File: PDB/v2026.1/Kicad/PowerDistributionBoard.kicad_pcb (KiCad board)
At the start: 2 copper layers, 184.8 x 112.4 mm, 78 parts, among them J1 12V_EXP3, J10 BMS, J11 IMD, J12 Suspension_Linear_Pot1, J13 Suspension_Linear_Pot2, J14 Suspension_Linear_Pot3, J15 Suspension_Linear_Pot4, J16 CCM_Faults, J17 EXP1_5V, J18 RasPI_5V, J19 LATCH_12V, J2 12V_EXP2, J20 Throttle_Sensor, J21 Current_Sensor, J22 Brake_Sensor1, J23 Brake_Sensor2, J24 Wheel_Sensor1, J25 Wheel_Sensor2, J26 3V3_EXP, J27 BATTERY_12V, J28 BATTERY_GND, J29 BATTERY_24V, J3 12V_EXP1, J31 FAN1_24V, J32 FAN2_24V, J33 PUMP1_24V, J34 PUMP2_24V, J35 24V_EXP1, J4 RTM, J5 CCM_12V, J7 BSPD, J8 LATCH, J9 TSSI, M3 MountingHole M3, U1 5to3.3_Linear_Regulator, U2 TLV76150DCYR

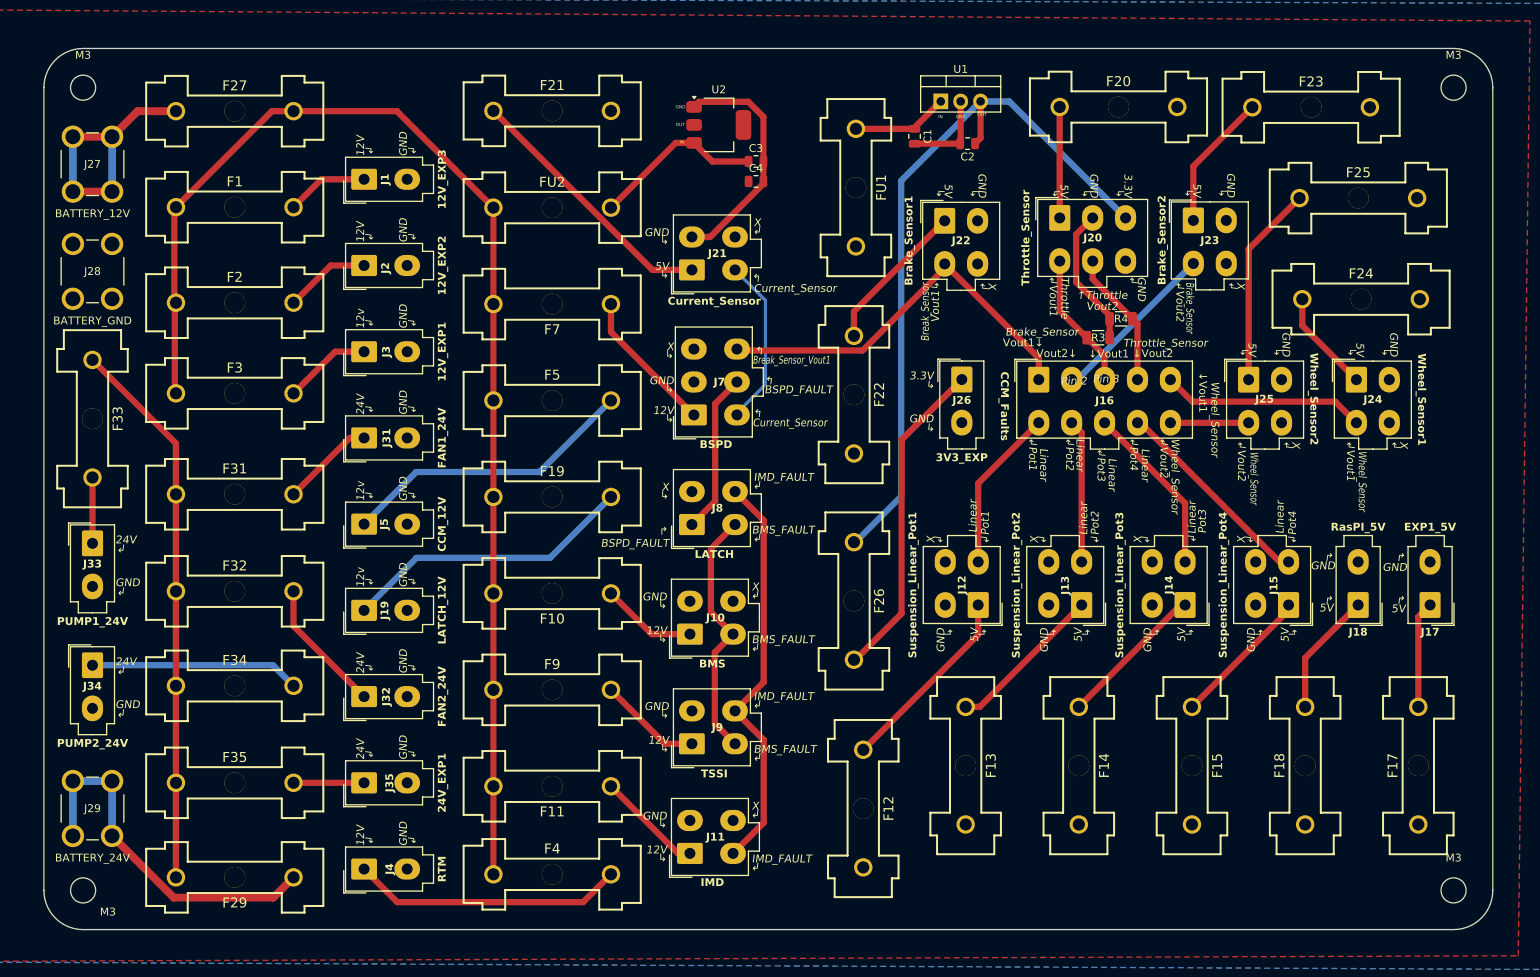
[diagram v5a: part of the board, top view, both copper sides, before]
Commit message: Combined break pressure into Throttle sensor
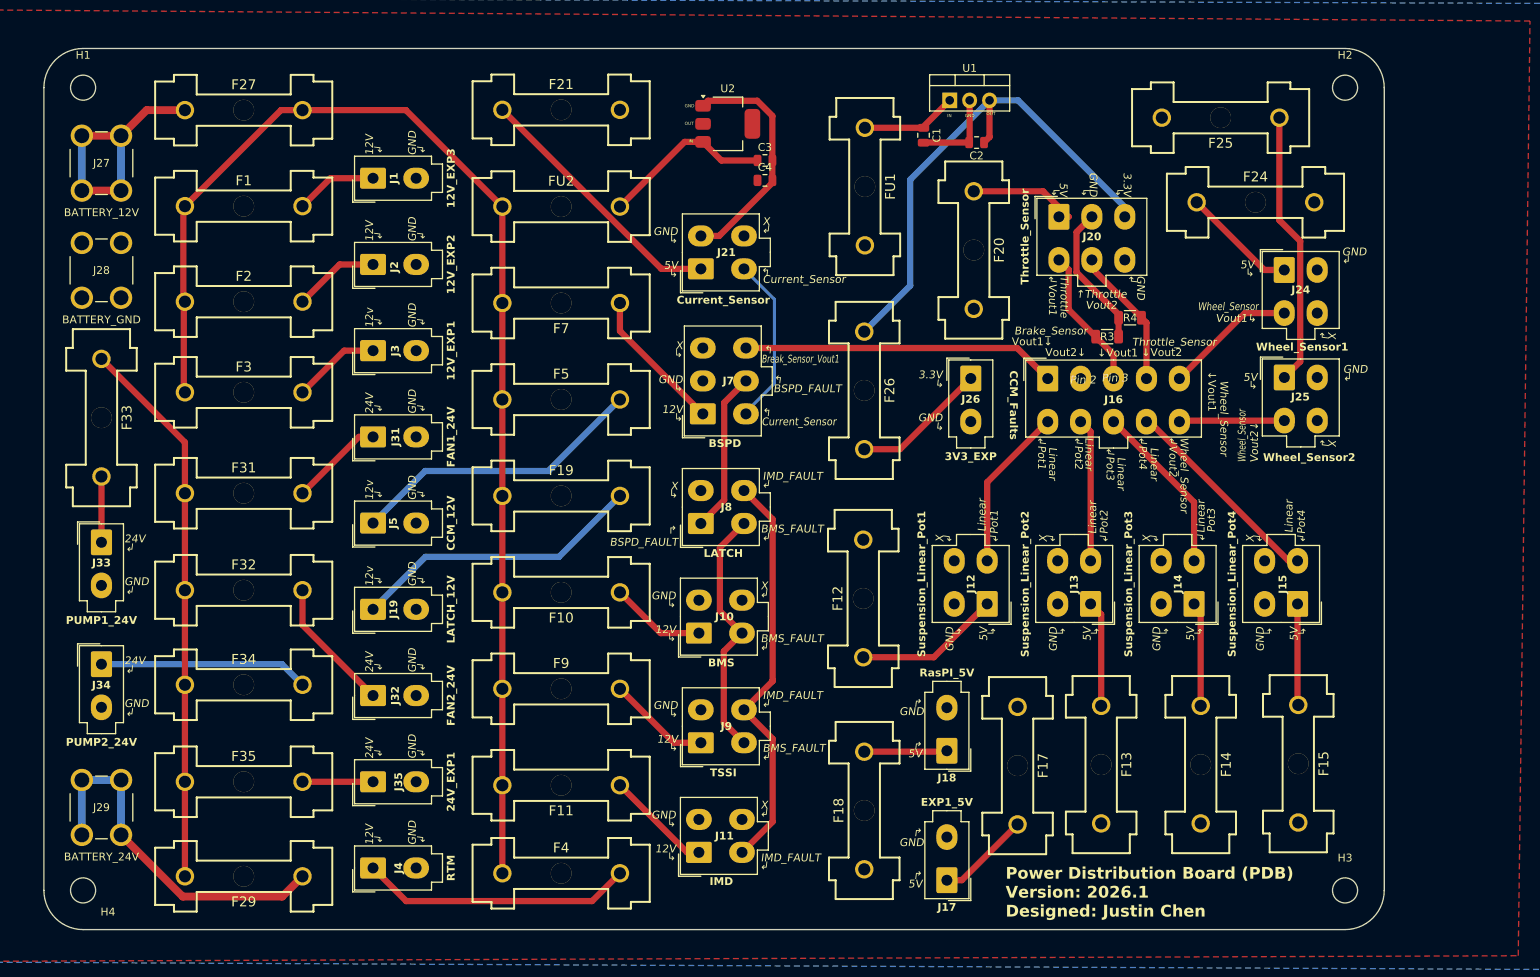
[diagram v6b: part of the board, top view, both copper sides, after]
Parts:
- removed F22, F23: 500mA, 0footprints:649-SERIES-HOLDER
- removed J22: Brake_Sensor1, 0footprints:Molex_Mini-Fit_Jr_5566-04A_2x02_P4.20mm_Vertical
- removed J23: Brake_Sensor2, 0footprints:Molex_Mini-Fit_Jr_5566-04A_2x02_P4.20mm_Vertical
- moved J17 70.9 mm to (165.4, 130.4)
- moved F18 56.5 mm to (154.8, 121.5)
- moved J18 55.7 mm to (165.4, 113.9)
- moved F17 51.1 mm to (174.4, 115.8), turned to 90 degrees
- moved F26 26.9 mm to (154.8, 67.9)
- moved F12 26.8 mm to (154.7, 94.5), turned to -90 degrees
- moved F20 26.0 mm to (168.8, 50.0), turned to 90 degrees
- moved F25 20.3 mm to (200.3, 33.1), turned to 0 degrees
- moved F24 18.3 mm to (204.7, 43.9)
- moved F13 17.3 mm to (185.0, 115.7)
- moved J24 16.7 mm to (208.4, 52.6)
- moved F14 15.6 mm to (197.7, 115.7)
- moved H2 13.8 mm to (216.2, 29.3)
- moved H3 13.8 mm to (216.2, 131.7)
- moved F15 13.6 mm to (210.2, 115.6)
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- renumbered M3 to H1, M3 to H2, M3 to H3, M3 to H4
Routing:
- net 3.3V: track 93.2 -> 65.9 mm
- net /Fuse_EXP_3V3: track 41.4 -> 17.3 mm
- net Brake_Sensor_Vout2: track 21.7 -> 0.00 mm
- net /Fuse_Break1: track 19.5 -> 0.00 mm
- net /Fuse_Break2: track 17.6 -> 0.00 mm
- net Brake_Sensor_Vout1: track 51.2 -> 40.1 mm
- net /Fuse_Wheel2: track 25.9 -> 35.1 mm
- net Wheel_Sensor_Vout1: track 26.0 -> 16.8 mm
- net /Fuse_Lin_Pot2: track 20.2 -> 13.6 mm
- net /Fuse_Lin_Pot1: track 24.5 -> 18.6 mm
- net /Fuse_Lin_Pot3: track 18.9 -> 13.4 mm
- net /Fuse_RasPI_5V: track 15.8 -> 10.6 mm
- net /Fuse_Lin_Pot4: track 18.1 -> 12.9 mm
- net Wheel_Sensor_Vout2: track 9.97 -> 13.5 mm
- net /Fuse_EXP1_5V: track 13.6 -> 11.9 mm
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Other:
- board size 184.8 x 112.4 mm -> 171 x 112.4 mm
- board text added: "Power Distribution Board (PDB) Version: 2026.1 Designed: Justin Chen"

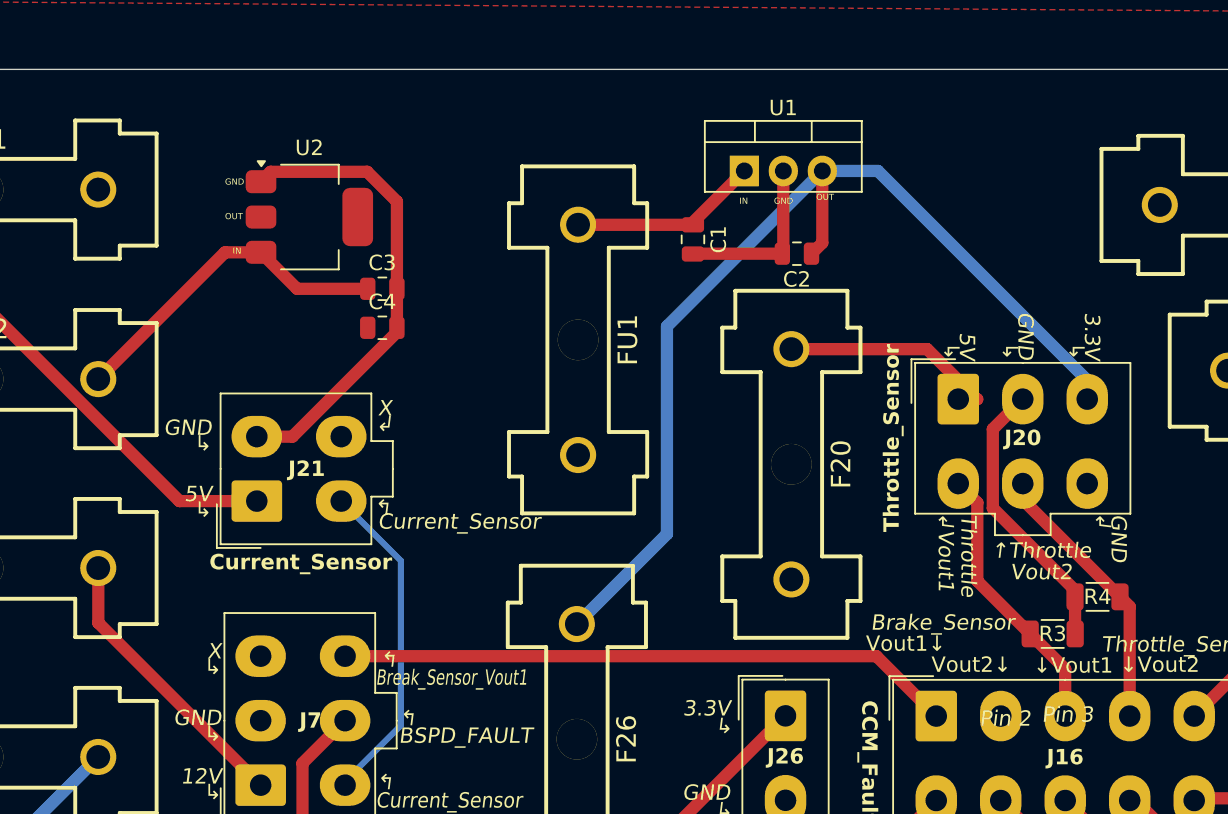
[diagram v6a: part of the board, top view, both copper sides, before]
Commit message: Added labels of possibly removeing 3V3 line
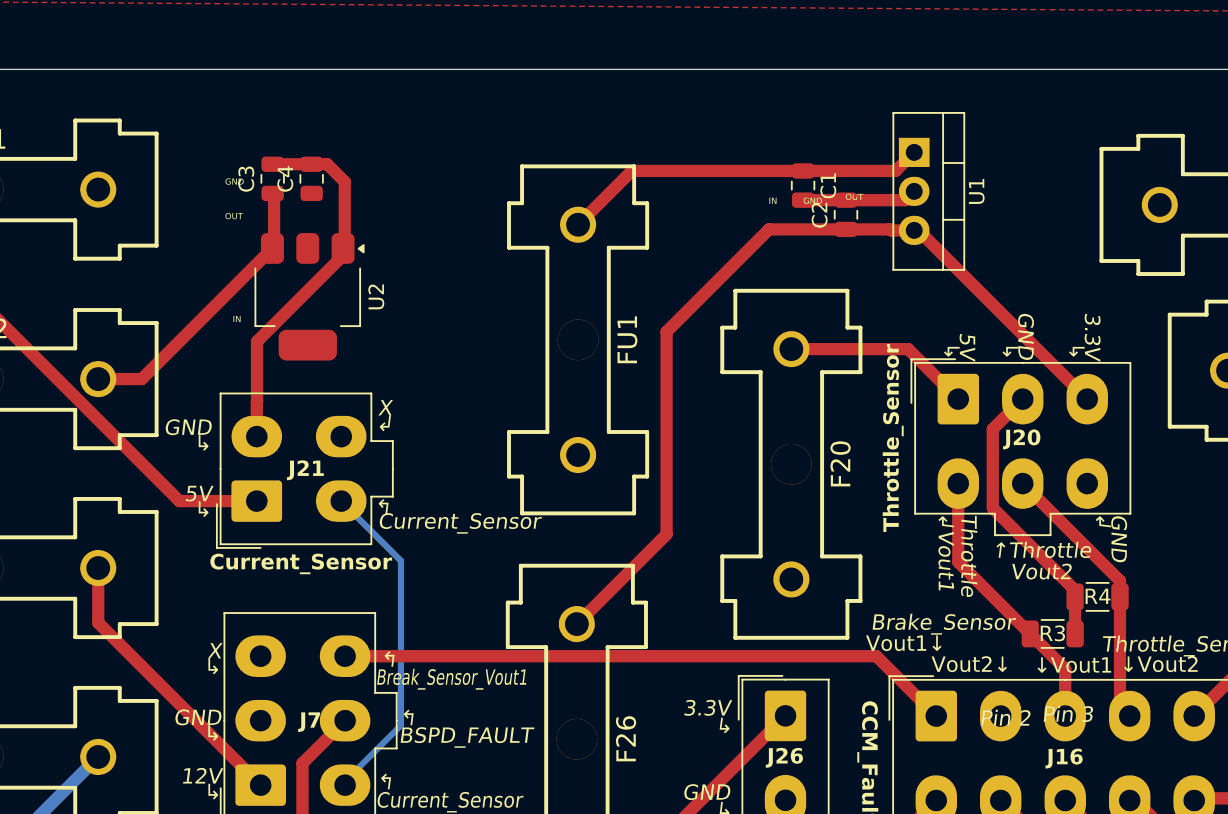
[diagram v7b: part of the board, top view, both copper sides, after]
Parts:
- moved U1 11.1 mm to (176.8, 29.7), turned to -90 degrees
- moved C4 10.7 mm to (137.5, 31.4), turned to 90 degrees
- moved C3 10.1 mm to (135.0, 31.4), turned to 90 degrees
- moved C1 7.98 mm to (169.5, 31.9)
- moved U2 5.20 mm to (137.3, 39.1), turned to -90 degrees
- moved C2 4.08 mm to (172.3, 33.8), turned to 90 degrees
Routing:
- net /Fuse_5to3.3: track 12.5 -> 23.9 mm
- net GND: track 60.3 -> 50.2 mm
- net 3.3V: track 65.9 -> 56.2 mm
- net /Fuse_12to5: track 22.0 -> 18.5 mm
- net /Fuse_Throttle: track 14.2 -> 12.2 mm

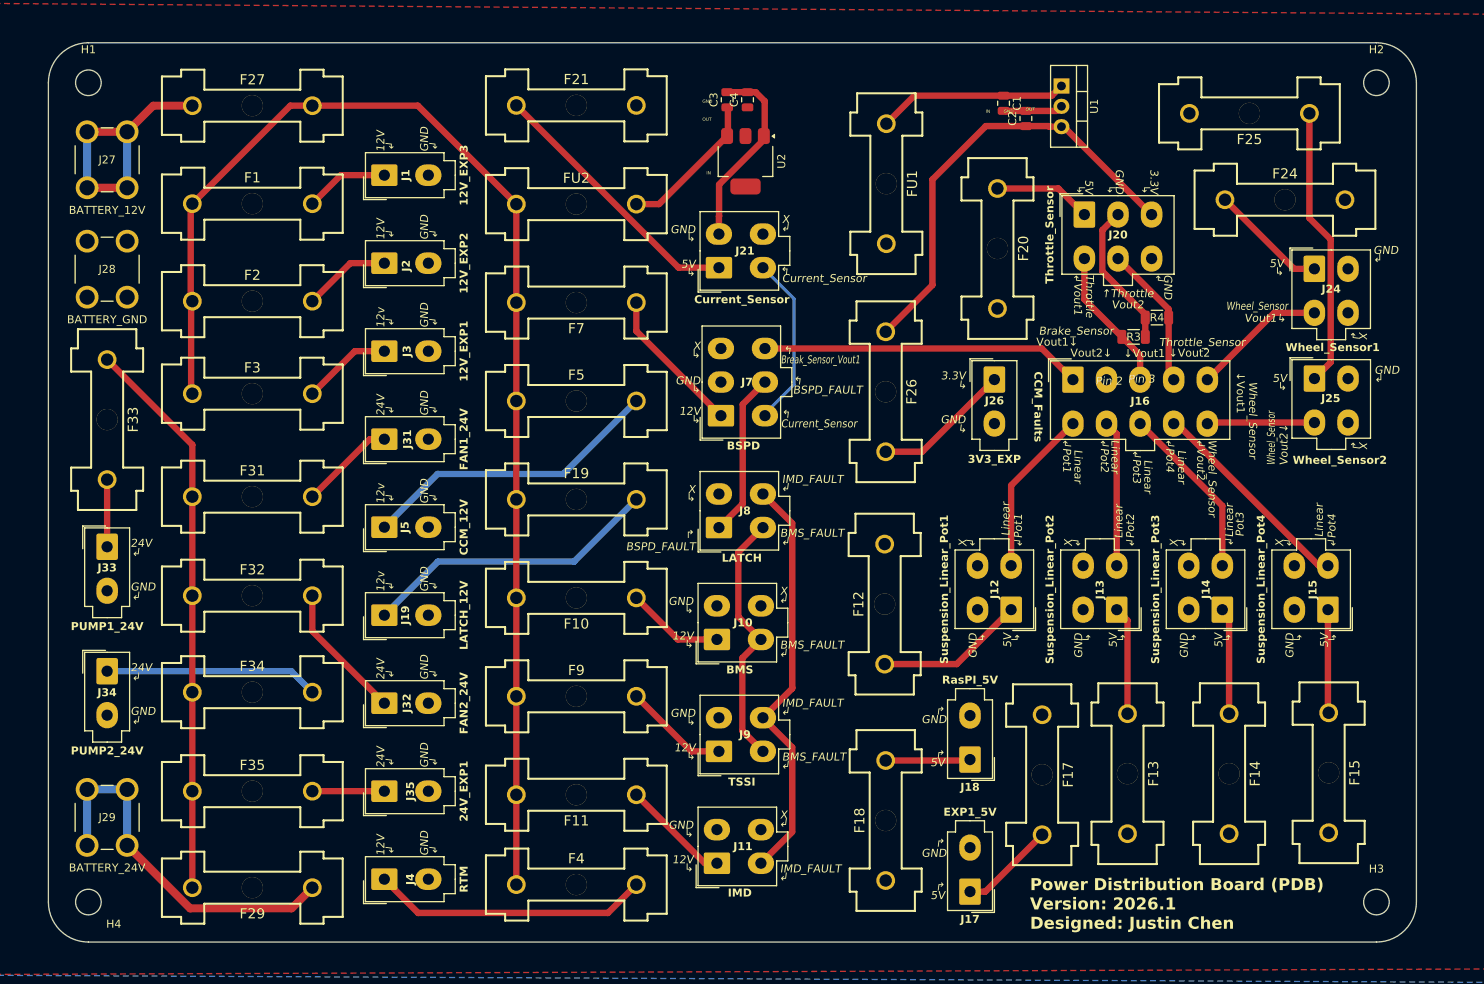
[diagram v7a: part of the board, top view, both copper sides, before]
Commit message: Added more silkscreen labels
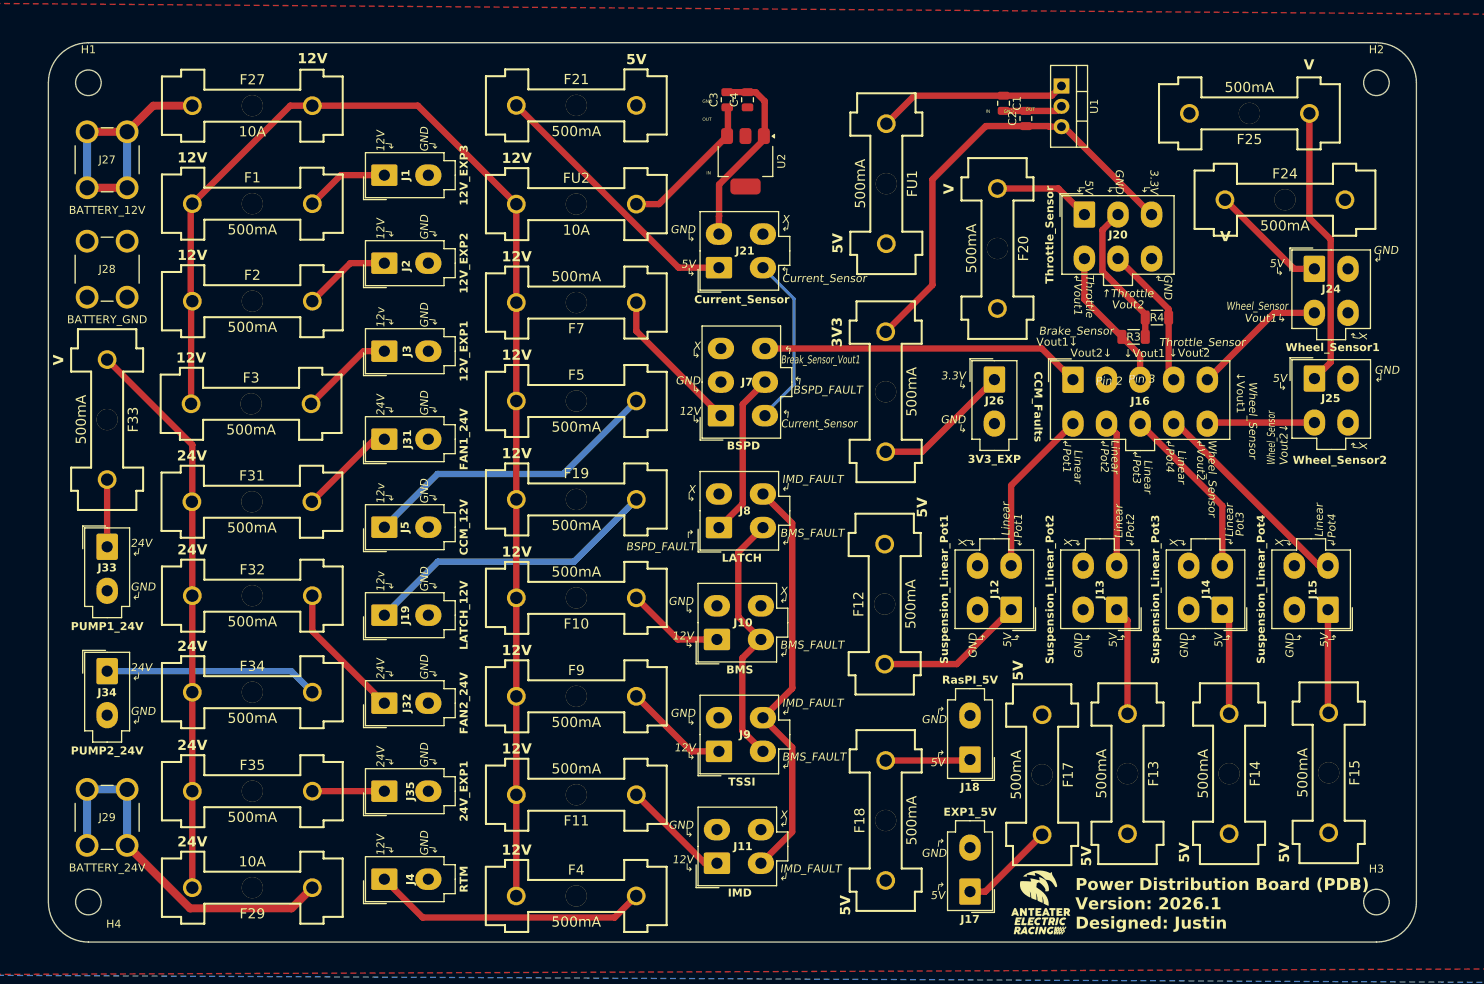
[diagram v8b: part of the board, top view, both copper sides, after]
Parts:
- added REF**: logo, 0footprints:logo, F.Cu at (174.0, 132.1)
- moved F4 1.42 mm to (116.1, 131.0)
- moved F3 1.27 mm to (75.5, 69.4)
- moved F31 0.64 mm to (75.6, 81.7)
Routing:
- net 12V: track 160.2 -> 162.9 mm
- net /Fuse_EXP1_12V: track 11.2 -> 11.9 mm
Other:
- board text added: "Power Distribution Board (PDB) Version: 2026.1 Designed: Justin"
- board text removed: "Power Distribution Board (PDB) Version: 2026.1 Designed: Justin Chen"
